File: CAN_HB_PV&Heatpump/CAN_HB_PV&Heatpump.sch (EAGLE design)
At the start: 58 parts, among them IC1 ULN2003AD, IC2 PCA82C250T, IC3 7805L, Q1 4.00000

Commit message: 
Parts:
- added C2: 100nF, rcl:C-EUC0805
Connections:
- net CAN_RX renamed RXCAN
- net CAN_TX renamed TXCAN
- net N$1 renamed DIN0+
- net N$21 renamed DIN0-
- net N$22 renamed DIN1+
- net N$24 renamed DIN1-
- net N$25 renamed DIN2+
- net N$27 renamed DIN2-
- net N$29 renamed DIN3-
- net N$30 renamed DIN3+
- net N$31 renamed DIN4+
- net N$33 renamed DIN4-
- net N$39 renamed DIN5-
- net N$40 renamed DIN5+
- net N$41 renamed DIN6+
- net N$43 renamed DIN6-
- net N$45 renamed DIN7-
- net N$46 renamed DIN7+
- removed net CH1: REL3G$2.O, U$2G$2.P$1
- removed net N$18: REL2G$2.P, U$4G$1.P$1
- removed net N$19: REL2G$2.O, U$4G$2.P$1
- new net N$1: REL3G$2.P, U$2G$2.P$1
- new net N$5: REL3G$2.S, U$2G$1.P$1
- new net N$6: REL2G$2.S, U$4G$1.P$1
- net +12V: now also C2.1
- net GND: now also C2.2
- net N$7: now also REL2G$2.P, U$4G$2.P$1; no longer REL3G$2.P, U$2G$1.P$1
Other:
- moved on the sheet: C1, C3, C4, C5, C6, C7, D0, D1, D2, D3, D4, D5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

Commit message: hardware finalized
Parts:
- R1, R10, R11, R12, R13, R14, R15, R16, R17, R18, R4, R6, R7, R9: device rcl:R-EU_R0603 -> rcl:R-EU_R0805
- R2, R5: value (none) -> 10k; device rcl:R-EU_R0603 -> rcl:R-EU_R0805

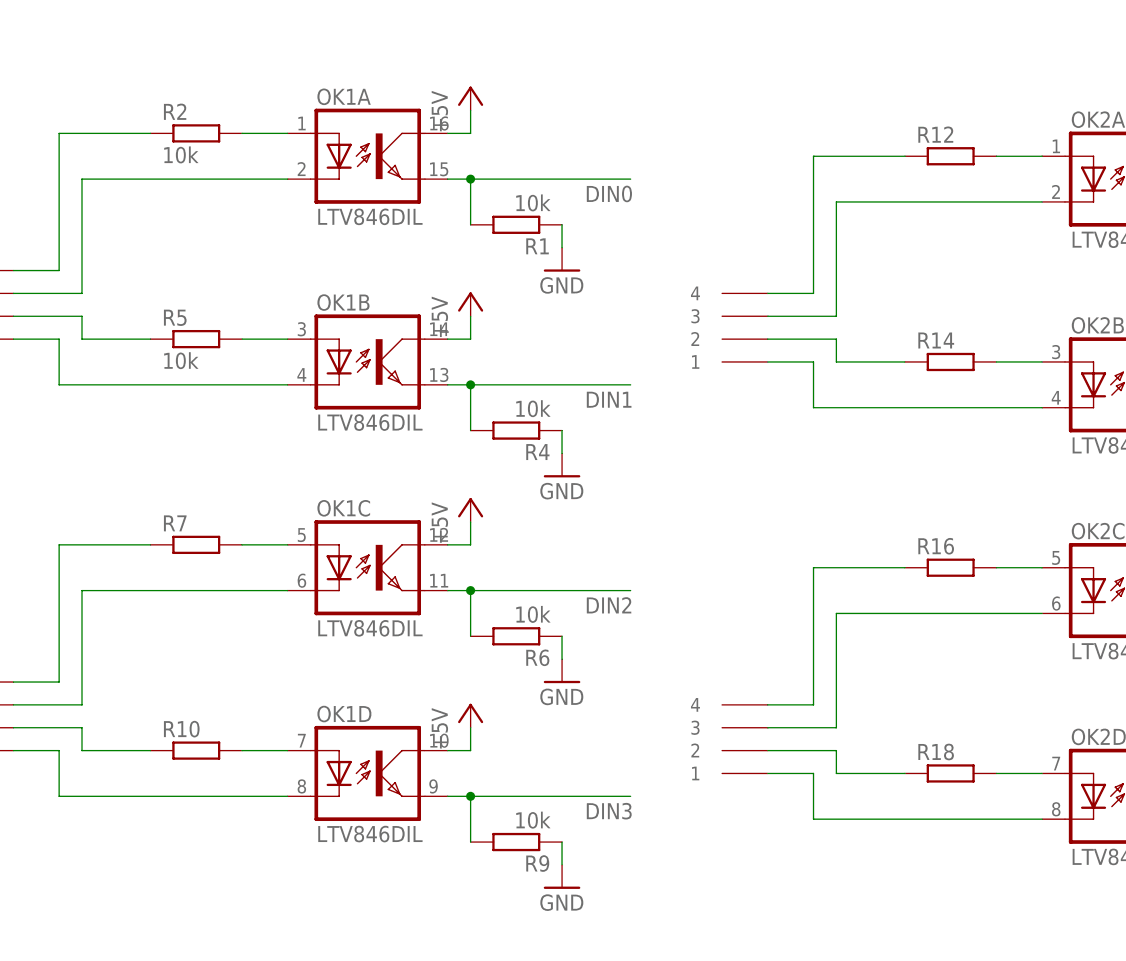
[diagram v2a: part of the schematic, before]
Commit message: PV_Heatpump Wiring plan added Firmware setup done
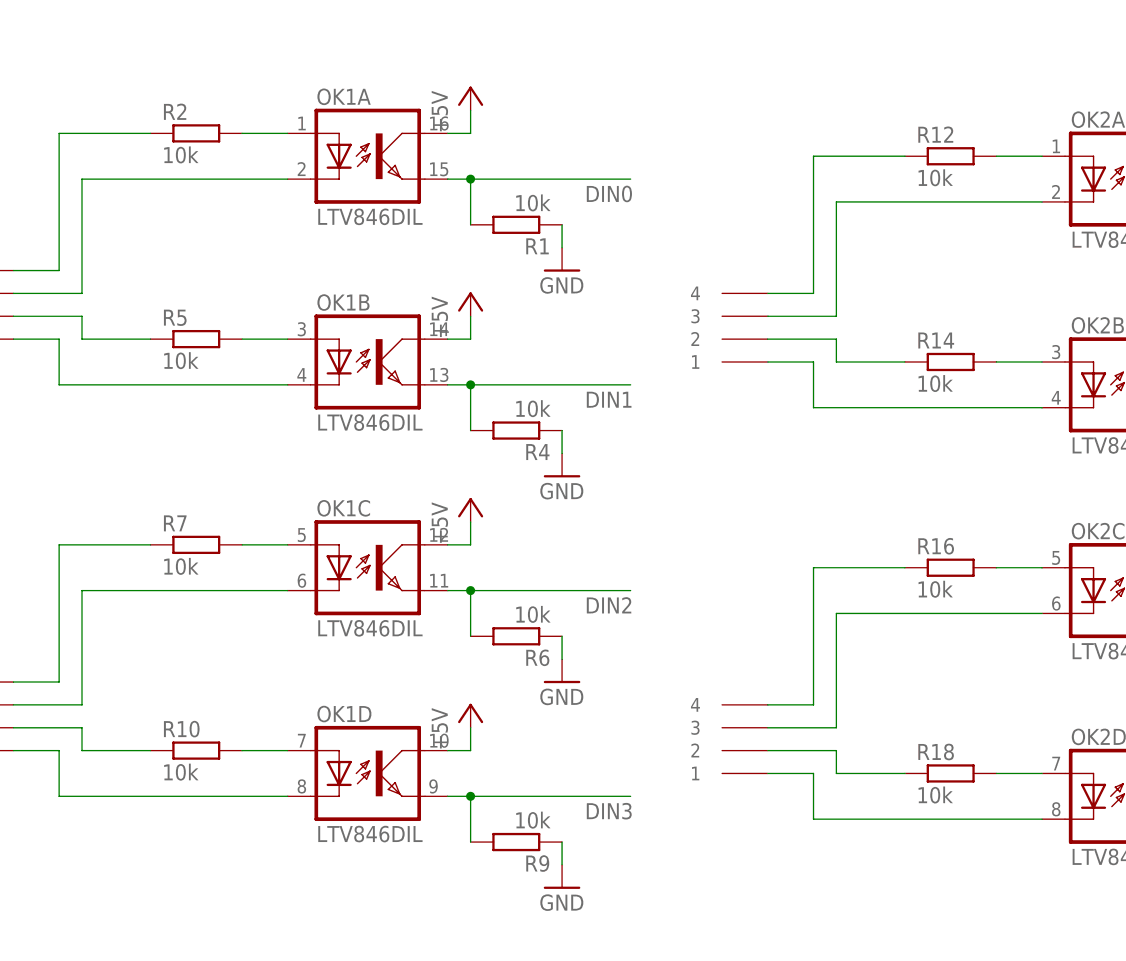
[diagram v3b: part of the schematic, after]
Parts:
- R10, R12, R14, R16, R18, R7: value (none) -> 10k
